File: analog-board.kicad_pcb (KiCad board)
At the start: 2 copper layers, 200 x 150 mm, 492 parts, among them J1 AC IN, J2 OUT, J3 CONN_20X2, P2 CONN_01X02, Q1 2N3906, Q10 2N3906, Q11 2N3906, Q12 2N3906, Q13 2N3906, Q14 2N3906, Q15 2N3906, Q16 2N3906, Q17 NPN, Q18 NPN, Q19 J111, Q2 2N3906, Q20 2N3906, Q3 2N3906, Q4 2N3906, Q5 2N3906, Q6 BCM857BS, Q7 2N3906, Q8 2N3906, Q9 2N3906, U1 LM13700, U10 ADR01, U11 DG212B, U12 DG212B, U13 DG408, U14 DG408, U15 TL072-, U16 DG408, U17 DG408, U18 LM13700, U19 LM13700, U2 LM13700, U21 TL072-, U22 TL074-, U23 TL074-, U24 TL074-, U25 TL074-, U26 TL072-, U27 TL074-, U28 TL074-, U29 LM13700, U3 LM13700, U30 LM13700, U31 TL074-, U32 LM13700, U33 TL074-, U34 TL074-, U35 TL074-, U36 74LV573, U38 0 - 10V, U39 TL074-, U4 DG212B, U40 DG419, U41 0 - 10V, U42 10 - 0V, U43 LM7812, U44 LM7912, U45 DG408, U46 7805, U5 TL074-, U6 AD5556, U7 TL072-, U8 TL074-, U9 AD8672

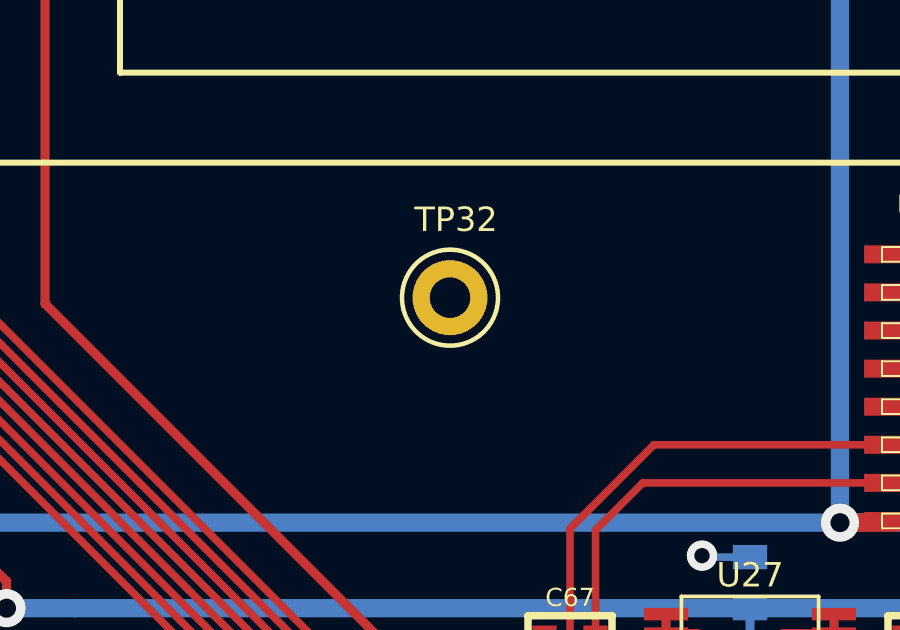
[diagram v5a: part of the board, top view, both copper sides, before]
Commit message: bottom silkscreen labelling of test points
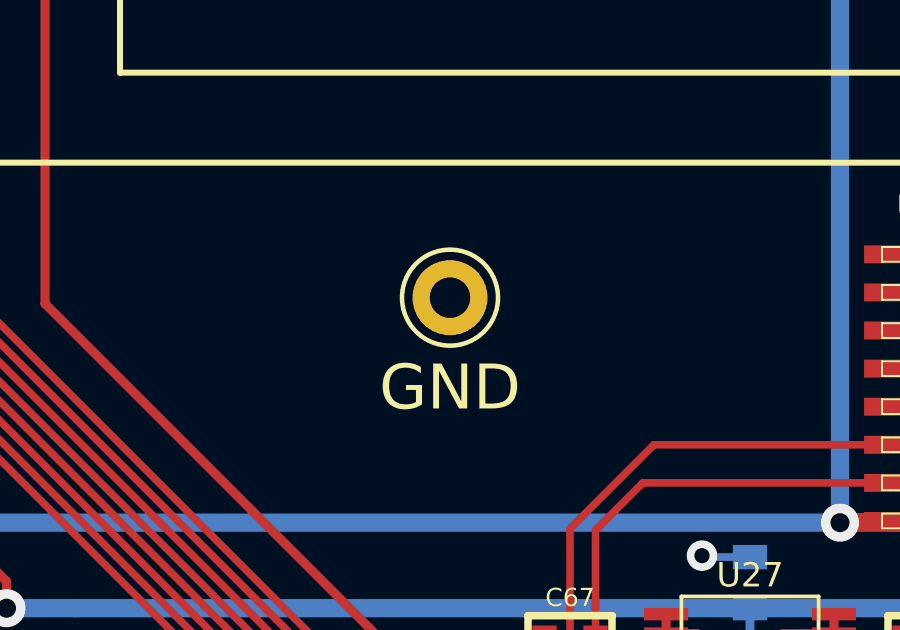
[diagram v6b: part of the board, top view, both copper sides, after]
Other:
- board text added: "CV IN"
- board text added: "GATE IN"
- board text added: "MIX OUT"
- board text added: "OFFSET ADJ NOISE LEVEL"
- board text added: "OFFSET ADJ OSC EG2"
- board text added: "OFFSET ADJ OSC LFO"
- board text added: "OFFSET ADJ OSCA FM"
- board text added: "OFFSET ADJ PWM EG2"
- board text added: "OFFSET ADJ PWM LFO"
- board text added: "OFFSET ADJ VCO1 LEVEL"
- board text added: "OFFSET ADJ VCO2 LEVEL"
- board text added: "OSCA GLIDE"
- board text added: "OSCB GLIDE"
- board text added: "PITCH"
- board text added: "S&H"
- board text added: "SMPL CLK"
- board text added: "VCO1 SUM"
- board text added: "VCO2 SUM"
- board text added: "VDAC"
- board text added: "VREF"

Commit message: silkscreen work done. Do footprint check and then order board
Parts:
- U42: moved to B.Cu
- moved U42 108.2 mm to (185.1, 140.4)
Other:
- board text added: "CV MIX OFFSET NULL"
- board text added: "FIL MOD CV SUM"
- board text added: "FIL MOD SCALE"
- board text added: "FIL MOD TRIM"
- board text added: "MonApollo ANALOG BOARD v1.0 03 2015"
- board text added: "OFFSET ADJ FIL EG2"
- board text added: "OFFSET ADJ FIL KEYTRACK"
- board text added: "OFFSET ADJ FIL LFO"
- board text added: "OFFSET ADJ FIL OSCB"
- board text added: "OFFSET ADJ VCA (TP24)"
- board text added: "OFFSET ADJ VCA LFO"
- board text added: "OFFSET ADJ VOL VCA"
- board text added: "RES CV TRIM"
- board text added: "SCALE"
- board text added: "VCA CV SUM"
